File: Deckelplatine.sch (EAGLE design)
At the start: 67 parts, among them IC1 MAX1487EESA+, IC2 74HCT595D, IC3 74HCT595D, IC4 74HCT595D, IC5 74HCT595D, IC6 74HCT595D, J1 52808-2570, Q1 BC846BSMD, Q2 BC846BSMD, U1 LM2676S, X1 236-406/000-023, X2 233-502

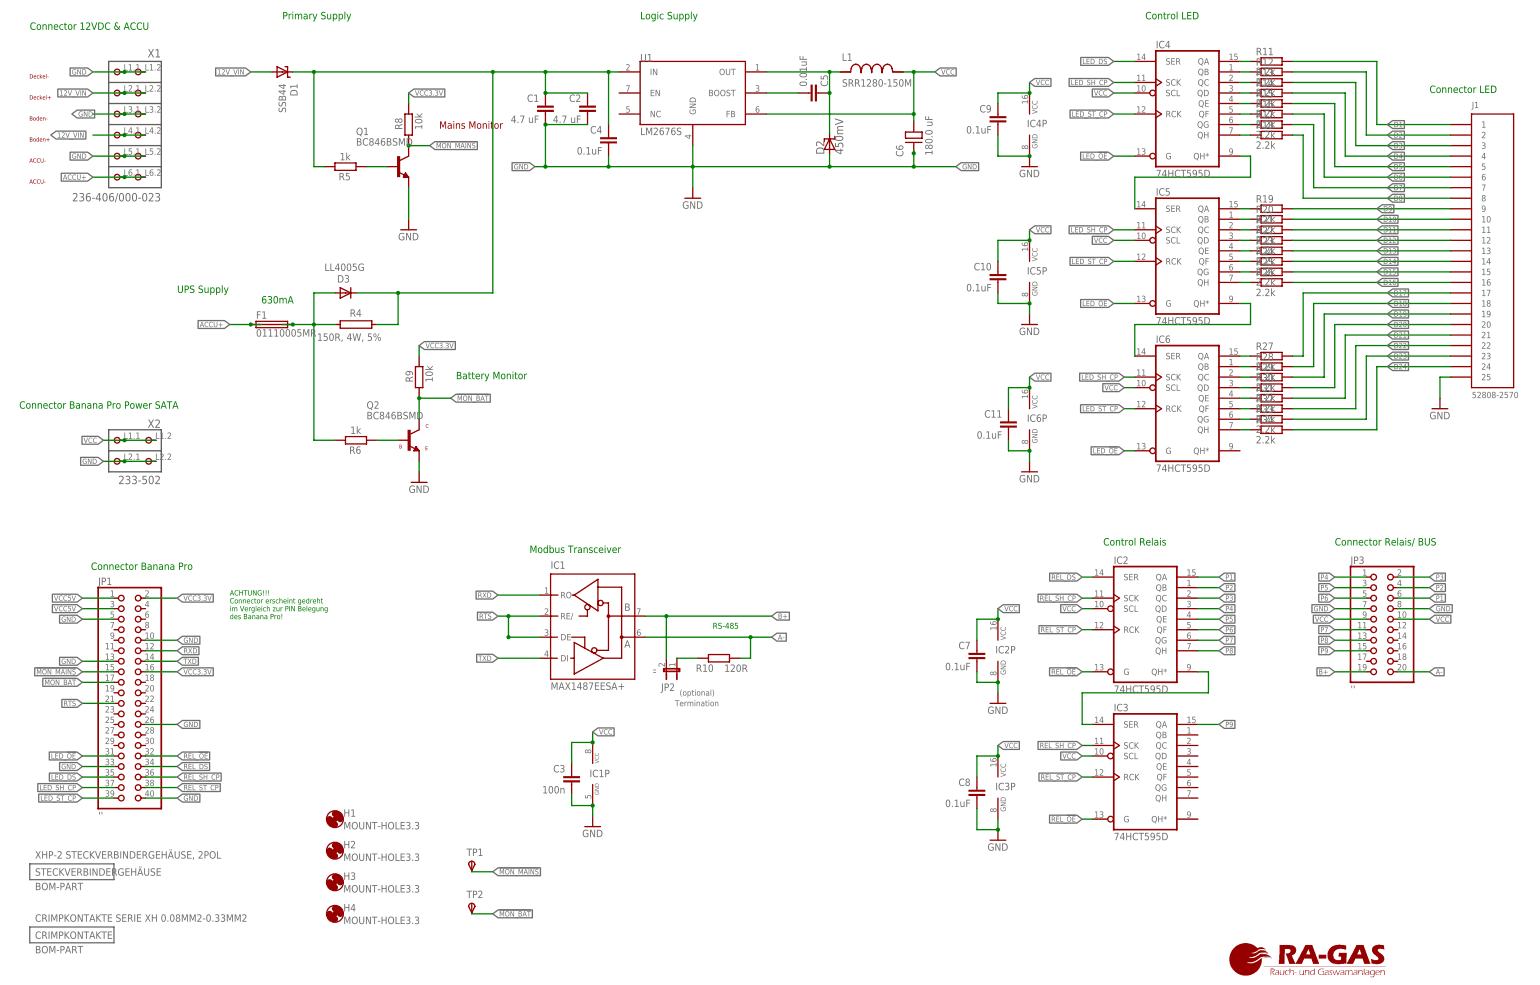
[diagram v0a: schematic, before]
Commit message: Dateinamen umbenannt, die Versionsnummer wird in Git geführt
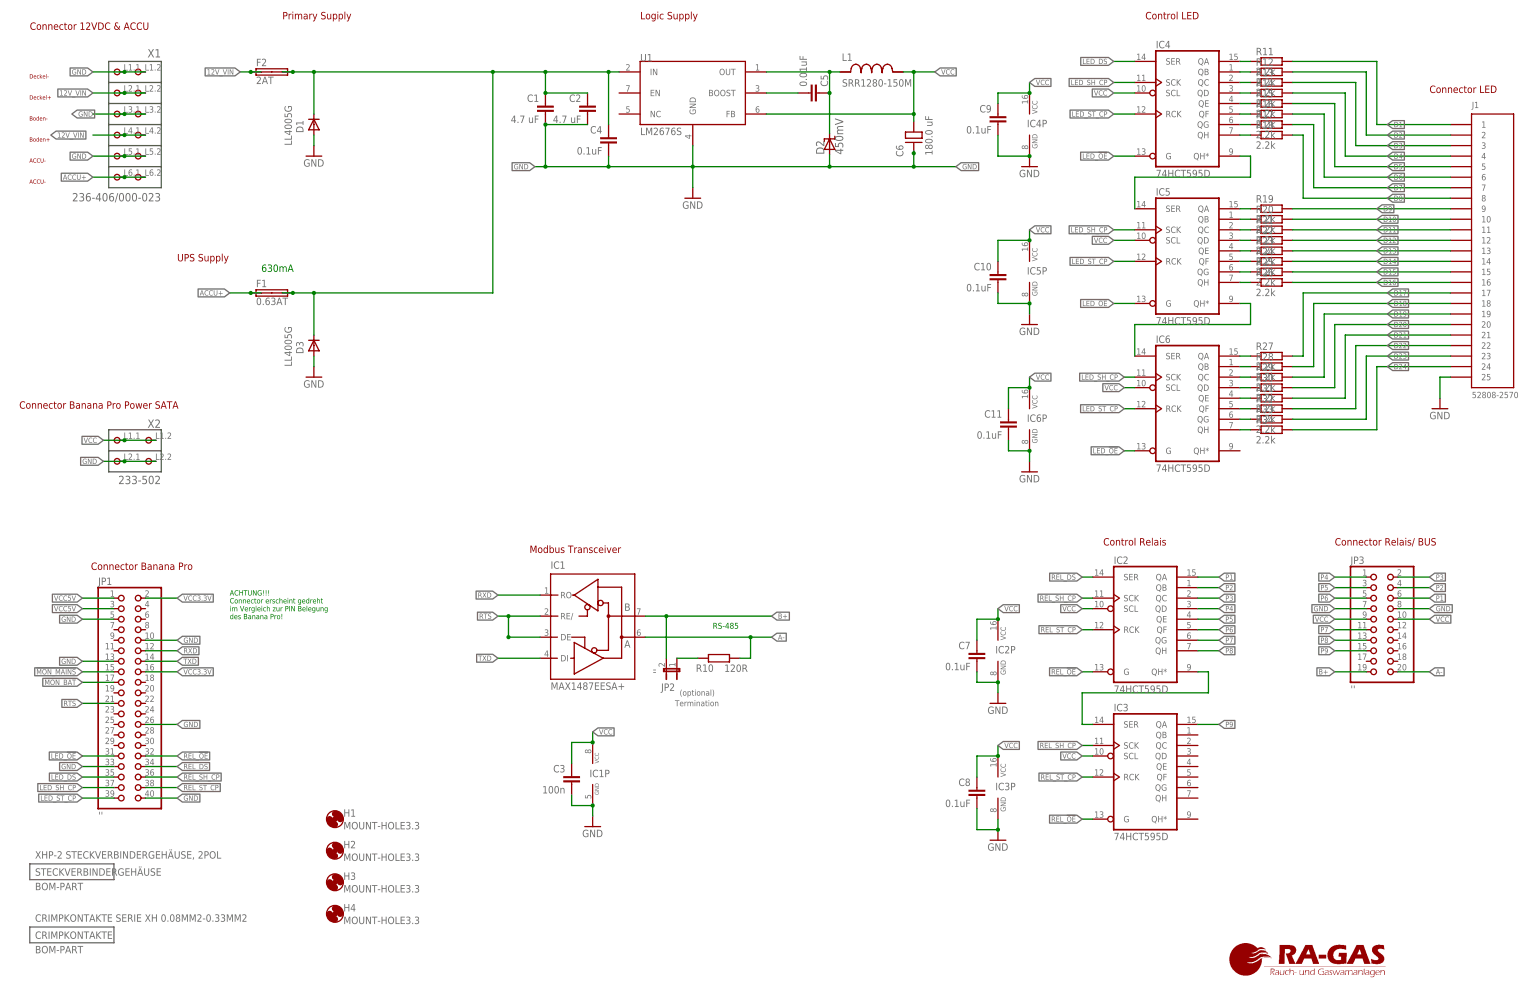
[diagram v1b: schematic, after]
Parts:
- removed Q1, Q2: BC846BSMD, transistor-npn:BC846BSMD
- removed R4: 150R, 4W, 5%, resistor-power:RKH206-8
- removed R5, R6: 1k, rcl:R-EU_R1210
- removed R8, R9: 10k, rcl:R-EU_R1210
- removed TP1, TP2: TPSB1,27, testpad:TPSB1,27
- added F2: 2AT, fuse-littlefuse:01110005MR
- D1: value SSB44 -> LL4005G; device diode:SUPPRESSOR-SMBJ -> diode:DIODE-MELF-MLL41; MF VISHAY -> TAIWAN SEMICONDUCTOR; MPN SSB44-E3/52T -> LL4005G; OC_FARNELL 1336557 -> 1625106
- F1: value 01110005MR -> 0.63AT
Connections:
- removed net N$37: Q1.B, R5.1
- net !MON_BAT: no longer Q2.C, R9.1, TP2.PP
- net !MON_MAINS: no longer Q1.C, R8.1, TP1.PP
- net 12V_VIN: now also F2.1A, F2.1B; no longer C1.1, C2.1, C4.1, D1.A, D1.C, D3.C, R4.2, R5.2, U1.IN
- net ACCU+: no longer D3.A, F1.2A, F1.2B, R4.1, R6.2
- net GND: now also D1.A, D3.A; no longer Q1.E, Q2.E
- net N$4: now also C1.1, C2.1, C4.1, D1.C, D3.C, F1.2A, F1.2B, F2.2A, F2.2B, U1.IN; no longer Q2.B, R6.1
- net VCC3.3V: no longer R8.2, R9.2
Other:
- note removed: "B"
- note removed: "Battery Monitor"
- note removed: "C"
- note removed: "E"
- note removed: "Mains Monitor"
- moved on the sheet: D3, F1
